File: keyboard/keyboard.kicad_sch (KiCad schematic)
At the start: 16 parts, among them J1 USB_B_Mini, SW1 RST, U1 ATmega32U4-A, Y1 16 MHz

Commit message: added mx style swithches to  the keyboard pcb
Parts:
- C1, C2, C3, C4, C5, C6, C7: footprint (none) -> Capacitor_SMD:C_0805_2012Metric
- F1: footprint (none) -> Diode_SMD:D_SOD-123
- J1: footprint (none) -> Connector_USB:USB_Mini-B_Lumberg_2486_01_Horizontal
- R1, R2, R3, R4: footprint (none) -> Resistor_SMD:R_0805_2012Metric
- SW1: footprint (none) -> Button_Switch_SMD:SW_SPST_EVPBF
- Y1: footprint (none) -> Crystal:Crystal_SMD_3225-4Pin_3.2x2.5mm
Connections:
- net +5V: no longer U1.24 (AVCC), U1.44 (AVCC)
- net GND: now also Y1.2, Y1.4; no longer U1.15 (GND), U1.23 (GND), U1.35 (GND), U1.43 (GND)
- net ROW0: now reaches U1.27 (PD7)
- net COL1: now reaches U1.28 (PB4)
- net COL0: now reaches U1.29 (PB5)
- net ROW1: now reaches U1.30 (PB6)
- new net: U1.15 (GND), U1.23 (GND), U1.35 (GND), U1.43 (GND)
- new net: U1.24 (AVCC), U1.44 (AVCC)
- no-connect marks 2 -> 26
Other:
- added sheet keyboard matrix  (untitled.kicad_sch)

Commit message: changes to keyboard structure
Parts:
- C1, C2, C3, C4, C5, C6, C7: footprint Capacitor_SMD:C_0805_2012Metric -> (none)
- F1: footprint Diode_SMD:D_SOD-123 -> (none)
- J1: footprint Connector_USB:USB_Mini-B_Lumberg_2486_01_Horizontal -> (none)
- R1, R2, R3, R4: footprint Resistor_SMD:R_0805_2012Metric -> (none)
- SW1: footprint Button_Switch_SMD:SW_SPST_EVPBF -> (none)
- Y1: footprint Crystal:Crystal_SMD_3225-4Pin_3.2x2.5mm -> (none)
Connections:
- net +5V: now also U1.24 (AVCC), U1.44 (AVCC)
- net GND: now also U1.15 (GND), U1.23 (GND), U1.35 (GND), U1.43 (GND); no longer Y1.2, Y1.4
- net COL0: no longer names the net of U1.29 (PB5)
- net COL1: no longer names the net of U1.28 (PB4)
- net ROW0: no longer names the net of U1.27 (PD7)
- net ROW1: no longer names the net of U1.30 (PB6)
- no-connect marks 26 -> 2
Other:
- removed sheet keyboard matrix 

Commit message: added some more the the keyboard schematic
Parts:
- removed F1: 500mA, symbol Device:Polyfuse
- removed J1: USB_B_Mini, symbol Connector:USB_B_Mini
- added J1: USB_C_Receptacle_USB2.0, Connector_USB:USB_C_Receptacle_GCT_USB4105-xx-A_16P_TopMnt_Horizontal, symbol Connector:USB_C_Receptacle_USB2.0
- added R5: 5k1, Resistor_SMD:R_0603_1608Metric_Pad0.98x0.95mm_HandSolder, symbol Device:R_Small
- C1, C2, C3, C4, C5, C6, C7: footprint (none) -> Capacitor_SMD:C_0603_1608Metric_Pad1.08x0.95mm_HandSolder
- R1: value 10k -> 5k1; footprint (none) -> Resistor_SMD:R_0603_1608Metric_Pad0.98x0.95mm_HandSolder
- R2, R3, R4: footprint (none) -> Resistor_SMD:R_0603_1608Metric_Pad0.98x0.95mm_HandSolder
- SW1: footprint (none) -> Button_Switch_SMD:SW_SPST_PTS645
- Y1: footprint (none) -> Crystal:Crystal_SMD_3225-4Pin_3.2x2.5mm_HandSoldering
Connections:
- net +5V: now also J1.A4 (VBUS), J1.A9 (VBUS), J1.B4 (VBUS), J1.B9 (VBUS)
- net GND: now also Y1.2, Y1.4, J1.A1 (GND), J1.A12 (GND), J1.B1 (GND), J1.B12 (GND), R5.2
- net USB+: now also J1.A6 (D+), J1.B6 (D+)
- net USB-: now also J1.A7 (D-), J1.B7 (D-)
- net R2: now reaches U1.10 (PB2)
- net R3: now reaches U1.11 (PB3)
- net C2: now reaches U1.12 (PB7)
- net R4: now reaches U1.28 (PB4)
- net R5: now reaches U1.29 (PB5)
- net C1: now reaches U1.30 (PB6)
- net C3: now reaches U1.31 (PC6)
- net C4: now reaches U1.32 (PC7)
- net R1: now reaches U1.9 (PB1)
- net HWB: no longer names the net of U1.33 (~{HWB}/PE2)
- net HWB: no longer R1.1
- new net: J1.A5 (CC1), R1.1
- new net: J1.B5 (CC2), R5.1
- no-connect marks 2 -> 21
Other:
- added sheet switch matrix (SwitchMatrix.kicad_sch)
- note added: "USB ESD Protection?"
- moved on the sheet: C1, R2, R3, R4, SW1, U1

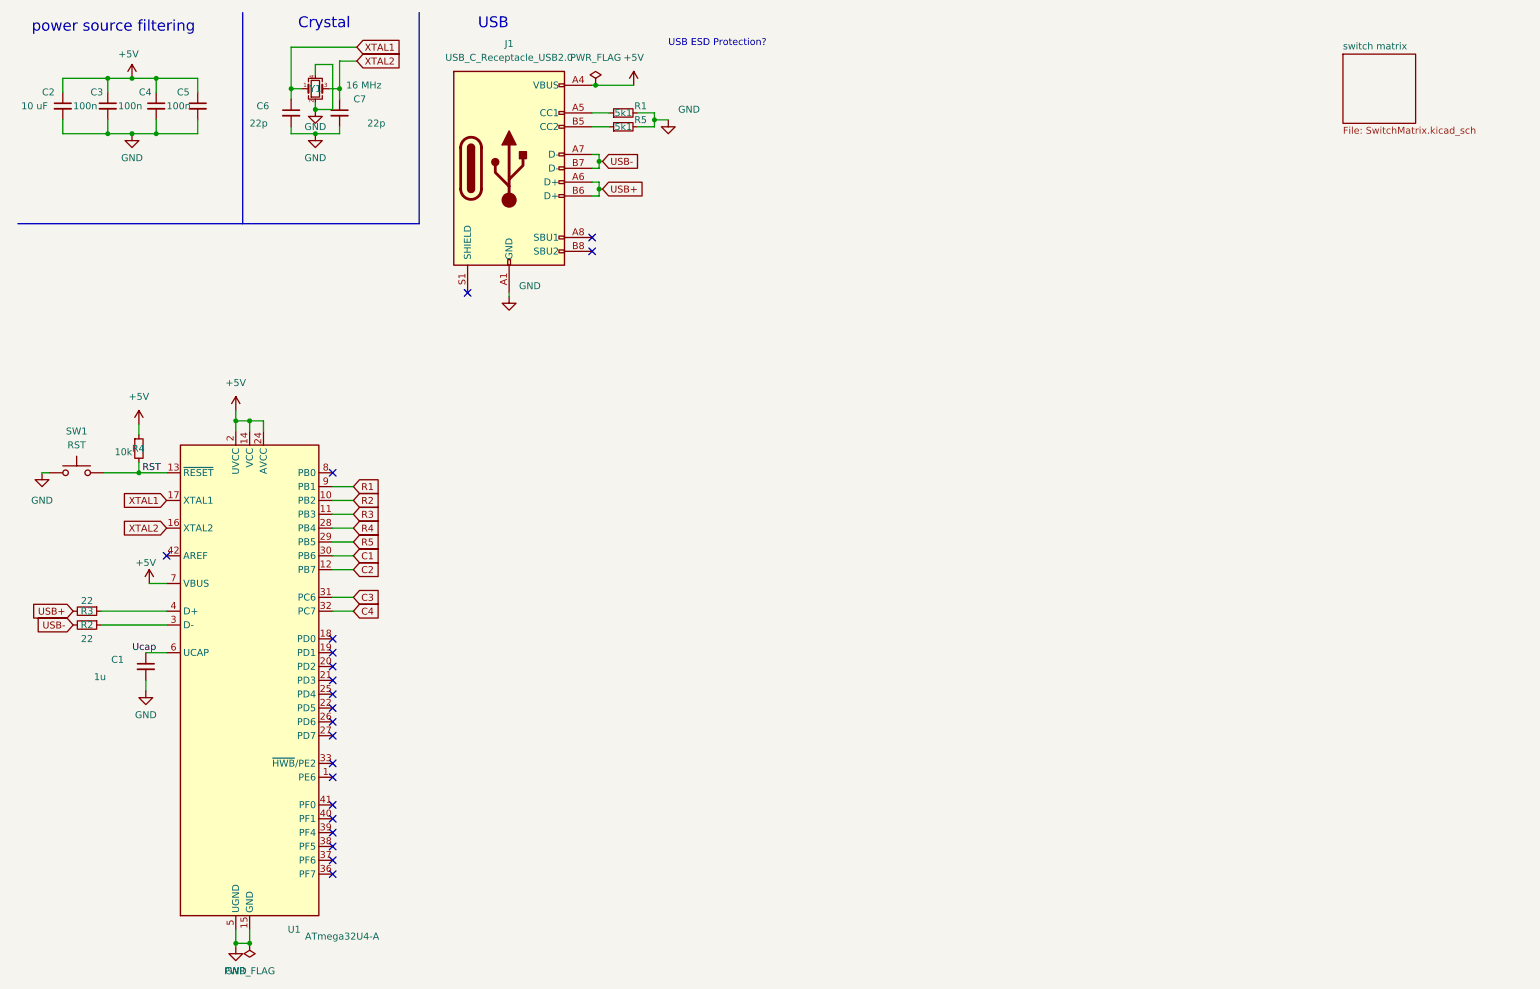
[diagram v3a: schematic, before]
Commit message: first iteration of the keyboard schematic
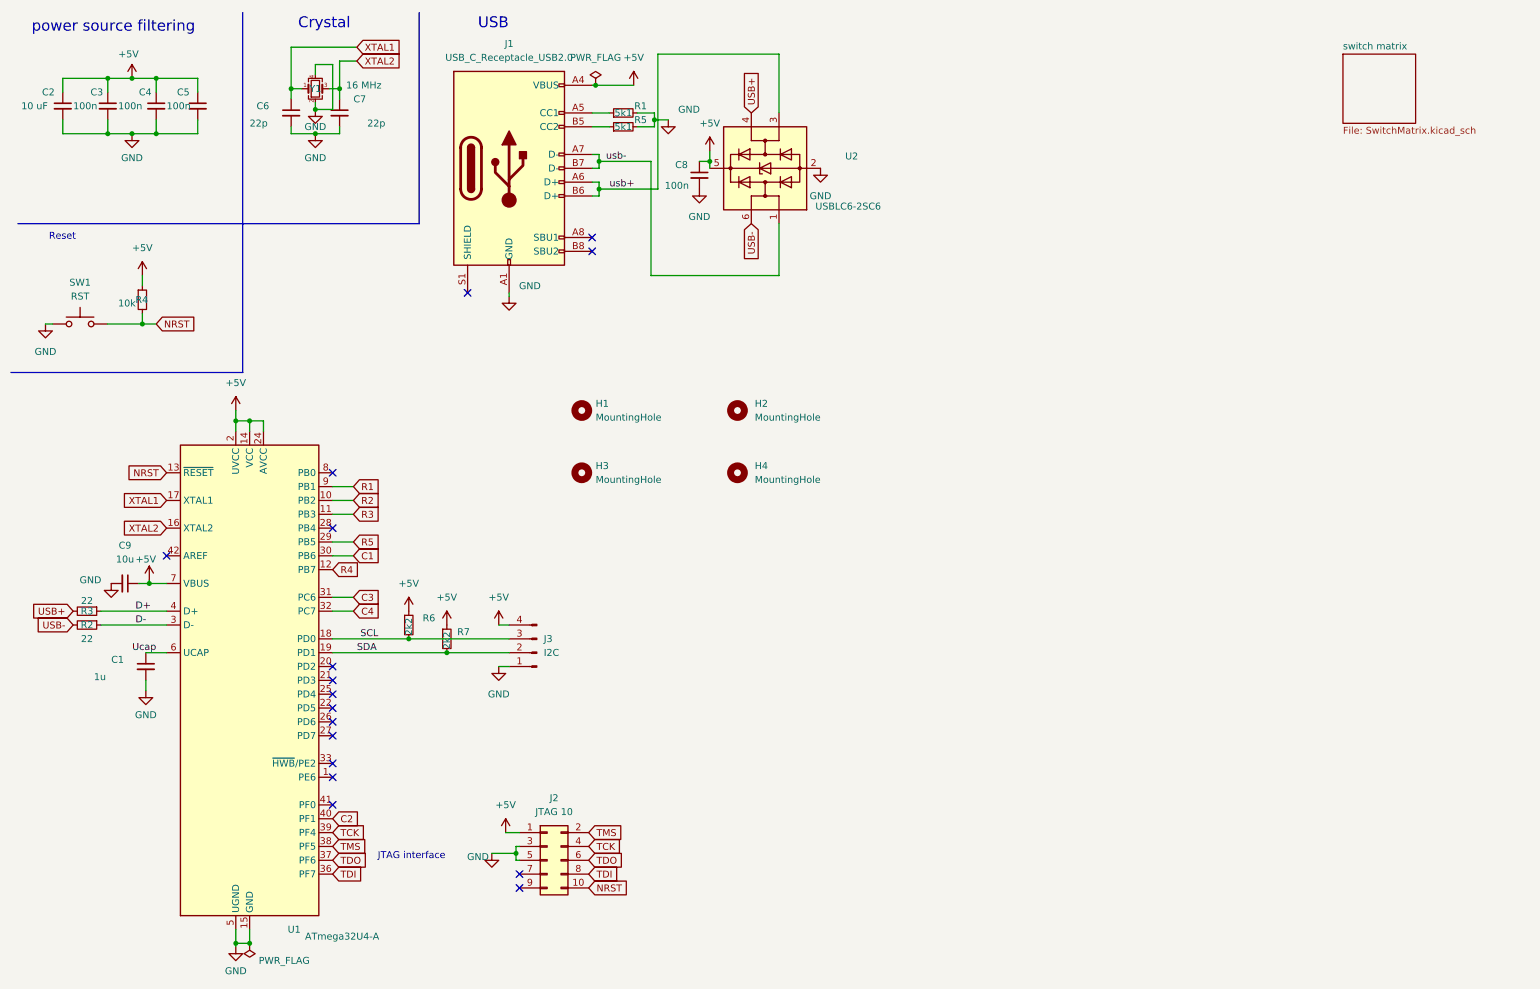
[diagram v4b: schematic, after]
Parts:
- added C8: 100n, Capacitor_SMD:C_0603_1608Metric_Pad1.08x0.95mm_HandSolder, symbol Device:C_Small
- added C9: 10u, Capacitor_SMD:C_0603_1608Metric_Pad1.08x0.95mm_HandSolder, symbol Device:C_Small
- added H1, H2, H3, H4: MountingHole, MountingHole:MountingHole_4.3mm_M4, symbol Mechanical:MountingHole
- added J2: JTAG 10, Connector_PinHeader_2.54mm:PinHeader_2x05_P2.54mm_Vertical, symbol Connector_Generic:Conn_02x05_Odd_Even
- added J3: I2C, Connector_PinHeader_2.54mm:PinHeader_1x04_P2.54mm_Vertical, symbol Connector:Conn_01x04_Pin
- added R6, R7: 2k2, Resistor_SMD:R_0603_1608Metric_Pad0.98x0.95mm_HandSolder, symbol Device:R_Small
- added U2: USBLC6-2SC6, Package_TO_SOT_SMD:SOT-23-6, symbol Power_Protection:USBLC6-2SC6
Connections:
- net +5V: now also C8.1, C9.1, J2.1 (Pin_1), J3.4 (Pin_4), R6.1, R7.1, U2.5 (VBUS)
- net C2: now also U1.40 (PF1); no longer U1.12 (PB7)
- net GND: now also C8.2, C9.2, J2.3 (Pin_3), J2.5 (Pin_5), J3.1 (Pin_1), U2.2 (GND)
- net R4: now also U1.12 (PB7); no longer U1.28 (PB4)
- net USB+: now also U2.4 (I/O2); no longer J1.A6 (D+), J1.B6 (D+)
- net USB-: now also U2.6 (I/O1); no longer J1.A7 (D-), J1.B7 (D-)
- net SCL: now reaches U1.18 (PD0)
- net SCL: now also J3.3 (Pin_3), R6.2
- net SDA: now reaches U1.19 (PD1)
- net SDA: now also J3.2 (Pin_2), R7.2
- net D-: now reaches R2.1, U1.3 (D-)
- net TDI: now reaches U1.36 (PF7)
- net TDI: now also J2.8 (Pin_8)
- net TDO: now reaches U1.37 (PF6)
- net TDO: now also J2.6 (Pin_6)
- net TMS: now reaches U1.38 (PF5)
- net TMS: now also J2.2 (Pin_2)
- net TCK: now reaches U1.39 (PF4)
- net TCK: now also J2.4 (Pin_4)
- net D+: now reaches R3.1, U1.4 (D+)
- net RST renamed NRST
- net NRST: now also J2.10 (Pin_10)
- new net usb+: J1.A6 (D+), J1.B6 (D+), U2.3 (I/O2)
- new net usb-: J1.A7 (D-), J1.B7 (D-), U2.1 (I/O1)
- no-connect marks 21 -> 17
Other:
- note added: "JTAG interface"
- note added: "Reset"
- note removed: "USB ESD Protection?"
- moved on the sheet: R4, SW1
